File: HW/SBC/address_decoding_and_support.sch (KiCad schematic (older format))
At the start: 9 parts, among them Q1 DS1813, SW1 RESET, U10 74LS138, U15 74LS74, U8 74HCT00, U9 74LS30, X1 8 MHz

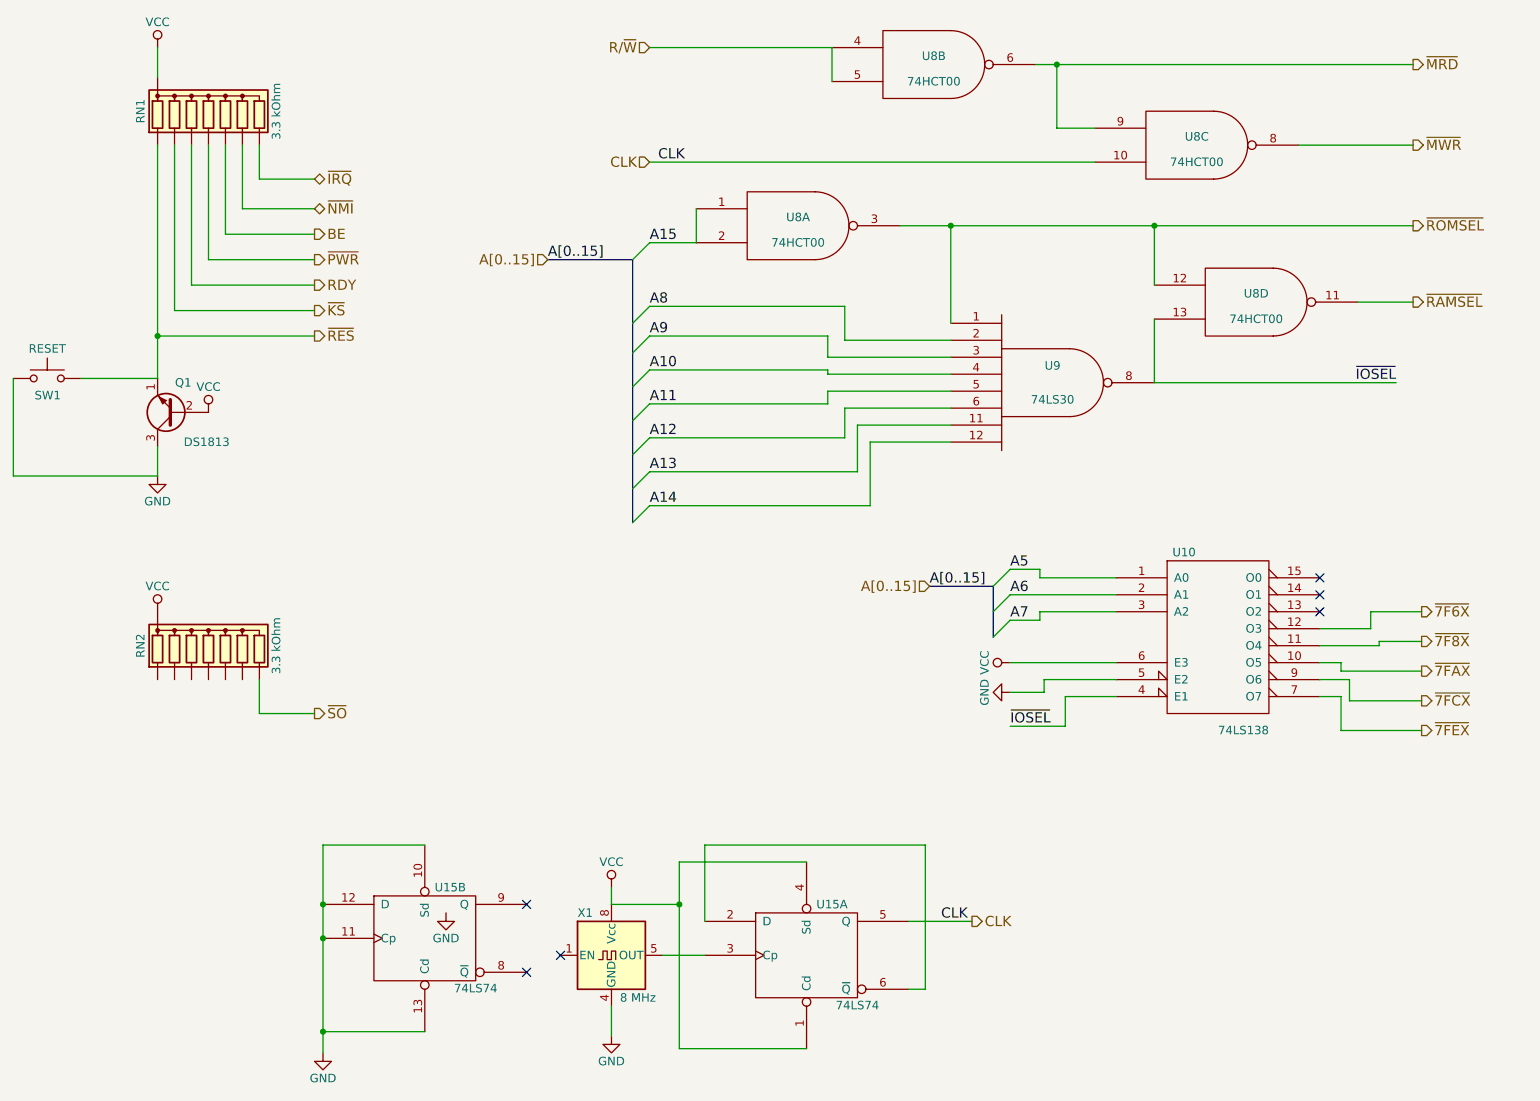
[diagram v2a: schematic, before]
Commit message: Small changes to schematics. Futher development of BIOS.
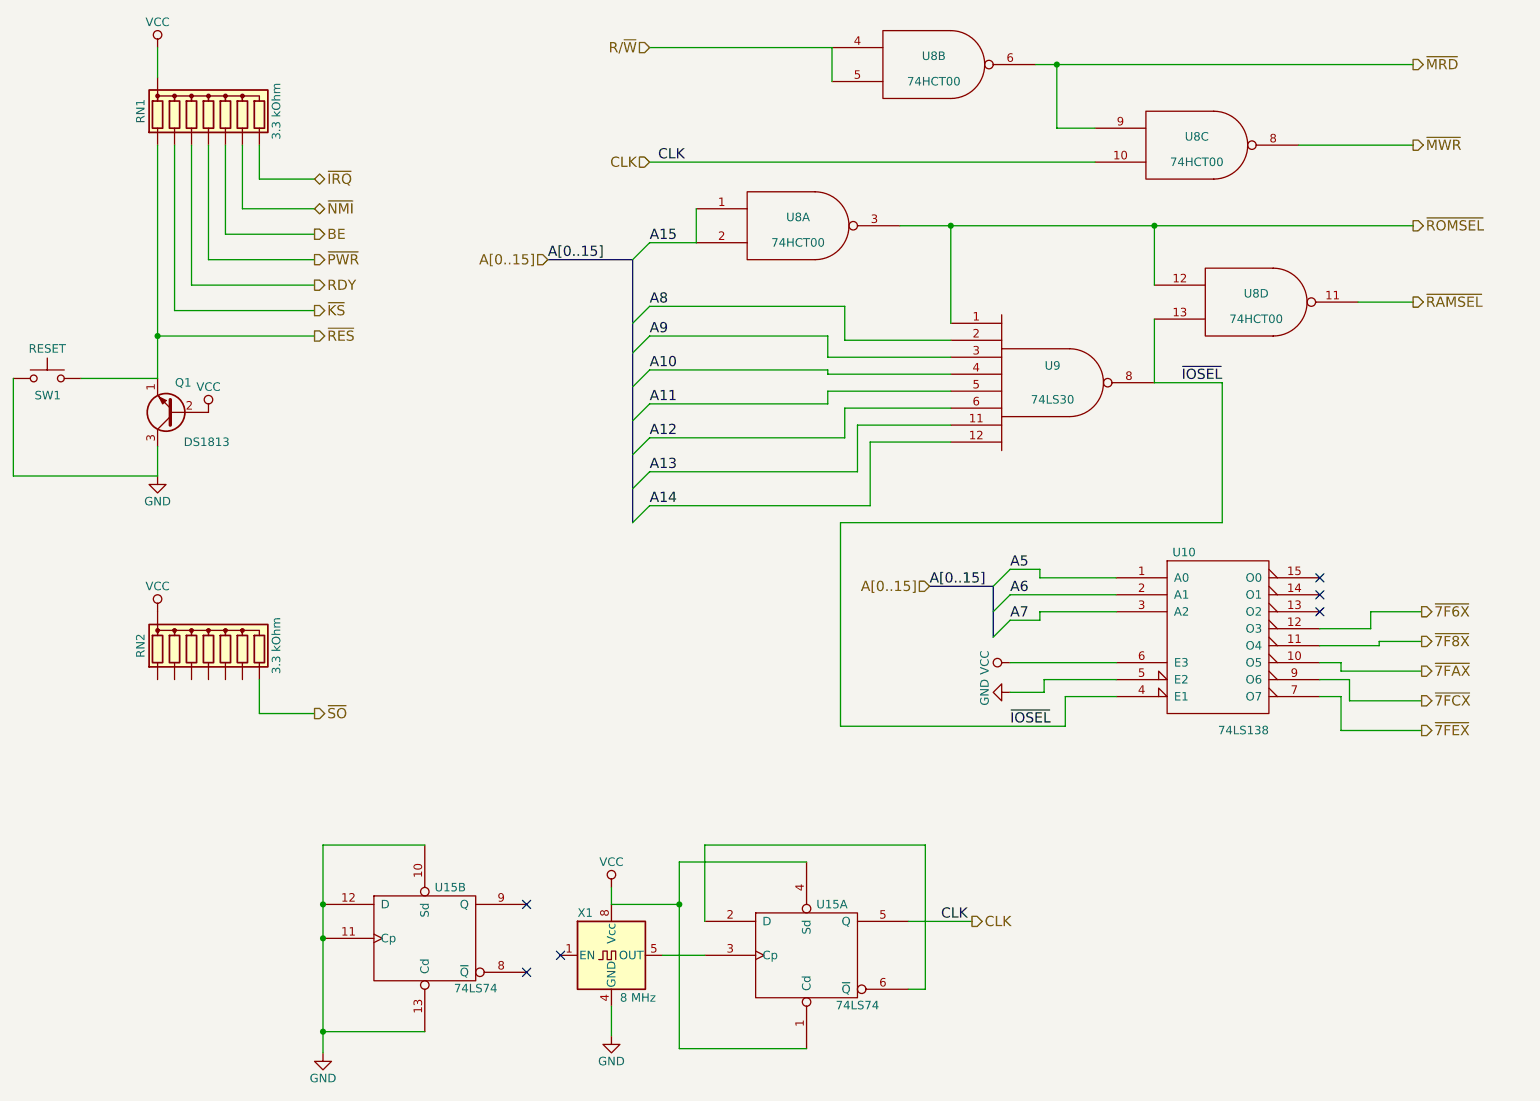
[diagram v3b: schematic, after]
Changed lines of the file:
@@
 LIBS:transistor
 LIBS:uln-ic
-LIBS:IDE_interface
+LIBS:+1.8V
+LIBS:+3.3V
+LIBS:+5V
+LIBS:+9V
+LIBS:25AA02EXXX-XOT
+LIBS:74LVC8T245
+LIBS:4021
+LIBS:7408
+LIBS:74125
+LIBS:74138
+LIBS:74148
+LIBS:74151
+LIBS:74157
+LIBS:74541
+LIBS:ANT
+LIBS:AP6502
+LIBS:AUDIO-JACK-3
+LIBS:AUDIO-JACK-6
+LIBS:BATTERY
+LIBS:BELFUSE-08B0-1X1T-06-F
+LIBS:C
+LIBS:CP
+LIBS:CRYSTAL
+LIBS:CRYSTAL-14
+LIBS:CVAR
+LIBS:DIODE
+LIBS:DIODES-AP3211
+LIBS:DIODESCH
+LIBS:DIODEZENER
+LIBS:DMMT5401
+LIBS:EDISON-BULB-E10
+LIBS:EDISON-SOCKET-E10
+LIBS:ENC28J60
+LIBS:FTDI-PLUG
+LIBS:GNDPWR
+LIBS:~GNDPWR
+LIBS:INDUCTOR
+LIBS:INTEL-EDISON-COMPUTE-MODULE
+LIBS:IS31AP4066D
+LIBS:JTAG
+LIBS:JTAG10
+LIBS:LATTICE-LC4256
+LIBS:LED
+LIBS:LED-BI
+LIBS:LED-BI-COMMON-CATHODE
+LIBS:LM324
+LIBS:LM1875
+LIBS:MAX3221
+LIBS:MC33926
+LIBS:MC34063A
+LIBS:MCP49X1
+LIBS:MCP3204
+LIBS:MECH
+LIBS:MIC2039
+LIBS:MIC2288
+LIBS:MICROSD-AMPHENOL-114-00841-68
+LIBS:MOSFET-N
+LIBS:MOSFET-N-123
+LIBS:MOSFET-N-134
+LIBS:MOSFET-P
+LIBS:NPN
+LIBS:nRF8001
+LIBS:NXPUDA1334ATS
+LIBS:OPAMP-DUAL
+LIBS:P01
+LIBS:P02
+LIBS:P03
+LIBS:P05
+LIBS:P06
+LIBS:P06-MOTOR
+LIBS:P08
+LIBS:P10
+LIBS:P22
+LIBS:P24
+LIBS:PHOTO_TRANSISTOR
+LIBS:PIEZO
+LIBS:PNP
+LIBS:POLYFUSE
+LIBS:POT
+LIBS:PWR_FLAG
+LIBS:QRE1113
+LIBS:R
+LIBS:RASPBERRYPI
+LIBS:RASPBERRYPI2
+LIBS:RBUS8
+LIBS:RN4020
+LIBS:ROBOT-P10-IO
+LIBS:RS-232-DB-9-DTE
+LIBS:SEN-SHT3x-DIS
+LIBS:SERVO
+LIBS:SI4737-C40-GM
+LIBS:SI4737-GU
+LIBS:SKYWORKS-AAT1217-3.3
+LIBS:SPDT
+LIBS:SPST
+LIBS:SPST-4PIN
+LIBS:SST25VF032B-S2A
+LIBS:SST26VF032B
+LIBS:ST-LIS3MDL
+LIBS:STM32-32PIN
+LIBS:STM32-48PIN
+LIBS:STM32-64PIN
+LIBS:STM32SWDUART
+LIBS:ST-SWD
+LIBS:ST-TDA7266
+LIBS:SWD
+LIBS:TCS3472
+LIBS:TI-ADS7866
+LIBS:TICC3000
+LIBS:TIREF30XX
+LIBS:TP
+LIBS:TS5A623157
+LIBS:TSV631
+LIBS:TVS-DIODE
+LIBS:TXB0108-PW
+LIBS:USBAB
+LIBS:Vcc
+LIBS:Vdd
+LIBS:VIN
+LIBS:VREG
+LIBS:VREG_VOUTCENTER
 LIBS:74xgxx
 LIBS:ac-dc
@@
 Text HLabel 9075 2600 2    60   Output ~ 0
 ~RAMSEL
-Text Label 8975 3075 2    60   ~ 0
+Text Label 7950 3075 2    60   ~ 0
 ~IOSEL
 Text Label 6700 5100 0    60   ~ 0
@@
 Connection ~ 7550 2150
 Wire Wire Line
-	7550 3075 8975 3075
+	7550 3075 7950 3075
 Wire Wire Line
 	7550 3075 7550 2700
@@
 	7025 4925 7025 5100
 Wire Wire Line
-	7025 5100 6700 5100
+	7025 5100 5700 5100
 Wire Wire Line
 	6900 4825 6900 4900
@@
 	3250 6900 2650 6900
 Connection ~ 2650 6900
-$Comp
-L GND #PWR37
-U 1 1 5948F014
-P 3375 6200
-F 0 "#PWR37" H 3375 5950 50  0001 C CNN
-F 1 "GND" H 3375 6050 50  0000 C CNN
-F 2 "" H 3375 6200 50  0001 C CNN
-F 3 "" H 3375 6200 50  0001 C CNN
-	1    3375 6200
-	1    0    0    -1
-$EndComp
 Text HLabel 2600 2650 2    60   Output ~ 0
 ~KS
@@
 	2275 5025 2600 5025
 $Comp
-L VCC #PWR?
+L VCC #PWR33
 U 1 1 594C1459
 P 1675 1100
-F 0 "#PWR?" H 1675 950 50  0001 C CNN
+F 0 "#PWR33" H 1675 950 50  0001 C CNN
 F 1 "VCC" H 1675 1250 50  0000 C CNN
 F 2 "" H 1675 1100 50  0001 C CNN
@@
 $EndComp
 $Comp
-L GND #PWR?
+L GND #PWR37
 U 1 1 595DE156
 P 2650 7025
-F 0 "#PWR?" H 2650 6775 50  0001 C CNN
+F 0 "#PWR37" H 2650 6775 50  0001 C CNN
 F 1 "GND" H 2650 6875 50  0000 C CNN
 F 2 "" H 2650 7025 50  0001 C CNN
@@
 NoConn ~ 3850 6550
 NoConn ~ 4050 6450
+Wire Wire Line
+	7950 3075 7950 3900
+Wire Wire Line
+	7950 3900 5700 3900
+Wire Wire Line
+	5700 3900 5700 5100
 $EndSCHEMATC

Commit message: Changed all TTLs to HC family.
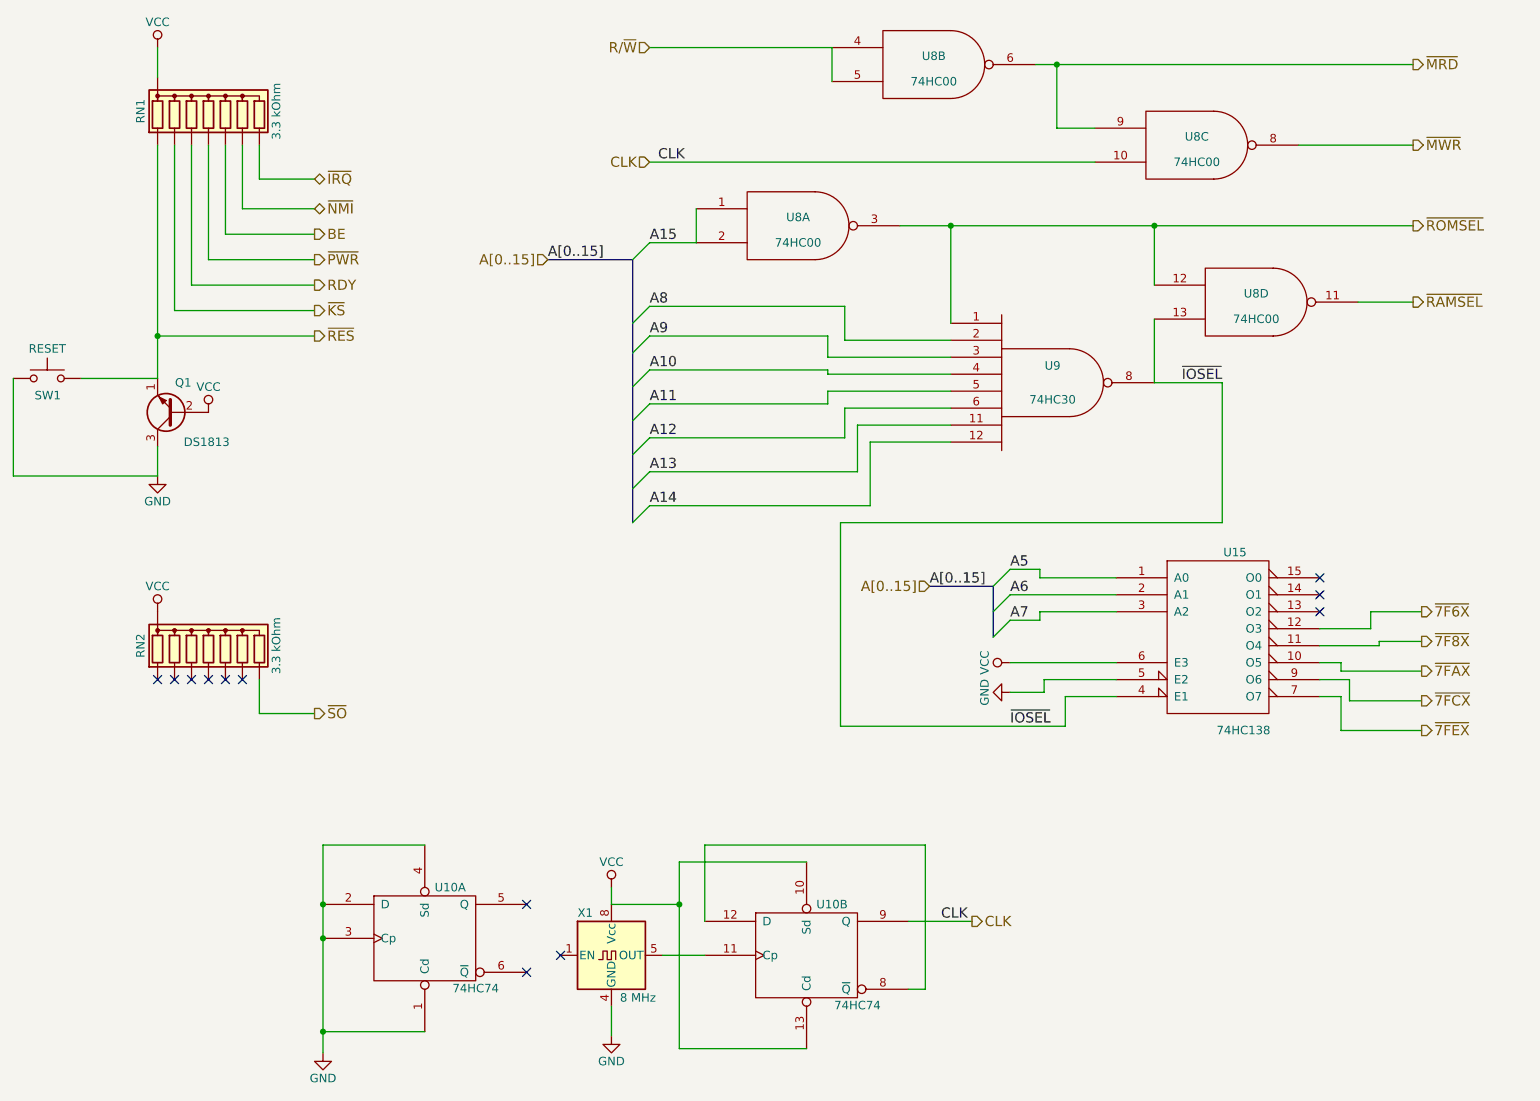
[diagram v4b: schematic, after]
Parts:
- removed U10: 74LS138, Housings_DIP:DIP-16_W7.62mm_Socket, symbol 74LS138
- removed U15: 74LS74, Housings_DIP:DIP-14_W7.62mm_Socket, symbol 74LS74
- removed U8: 74HCT00, Housings_DIP:DIP-14_W7.62mm_Socket, symbol 74HCT00
- removed U9: 74LS30, Housings_DIP:DIP-14_W7.62mm_Socket, symbol 74LS30
- added U10: 74HC74, symbol 74HC74
- added U15: 74HC138, symbol 74HC138
- added U8: 74HC00, symbol 74HC00
- added U9: 74HC30, symbol 74HC30
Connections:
- net A10: now also U9.4
- net A11: now also U9.5
- net A12: now also U9.6
- net A13: now also U9.11
- net A14: now also U9.12
- net A15: now also U8.1, U8.2
- net A5: now also U15.1 (A0)
- net A6: now also U15.2 (A1)
- net A7: now also U15.3 (A2)
- net A8: now also U9.2
- net A9: now also U9.3
- net CLK: now also U10.9 (Q), U8.10
- net GND: now also U10.1 (Cd), U10.2 (D), U10.3 (Cp), U10.4 (Sd), U10.7 (GND), U10.7 (GND), U15.5 (E2), U15.8 (GND), U8.7 (GND), U8.7 (GND), U8.7 (GND), U8.7 (GND), U9.7 (GND)
- net R/~W: now also U8.4, U8.5
- net VCC: now also U10.10 (Sd), U10.13 (Cd), U10.14 (VCC), U10.14 (VCC), U15.16 (VCC), U15.6 (E3), U8.14 (VCC), U8.14 (VCC), U8.14 (VCC), U8.14 (VCC), U9.14 (VCC)
- net ~7F6X: now also U15.12 (O3)
- net ~7F8X: now also U15.11 (O4)
- net ~7FAX: now also U15.10 (O5)
- net ~7FCX: now also U15.9 (O6)
- net ~7FEX: now also U15.7 (O7)
- net ~IOSEL: now also U15.4 (E1), U8.13, U9.8
- net ~MRD: now also U8.6, U8.9
- net ~MWR: now also U8.8
- net ~RAMSEL: now also U8.11
- net ~ROMSEL: now also U8.12, U8.3, U9.1
- net at X1.5 (OUT): now also U10.11 (Cp)
- new net: U10.12 (D), U10.8 (~Q)
- no-connect marks 6 -> 12
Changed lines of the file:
@@
 $EndDescr
-$Comp
-L 74HCT00 U8
-U 1 1 58D59B66
-P 5450 2150
-F 0 "U8" H 5450 2200 50  0000 C CNN
-F 1 "74HCT00" H 5450 2050 50  0000 C CNN
-F 2 "Housings_DIP:DIP-14_W7.62mm_Socket" H 5450 2150 50  0001 C CNN
-F 3 "" H 5450 2150 50  0001 C CNN
-	1    5450 2150
-	1    0    0    -1
-$EndComp
-$Comp
-L 74HCT00 U8
-U 4 1 58D59B7D
-P 8150 2600
-F 0 "U8" H 8150 2650 50  0000 C CNN
-F 1 "74HCT00" H 8150 2500 50  0000 C CNN
-F 2 "Housings_DIP:DIP-14_W7.62mm_Socket" H 8150 2600 50  0001 C CNN
-F 3 "" H 8150 2600 50  0001 C CNN
-	4    8150 2600
-	1    0    0    -1
-$EndComp
-$Comp
-L 74HCT00 U8
-U 2 1 58D59C3A
-P 6250 1200
-F 0 "U8" H 6250 1250 50  0000 C CNN
-F 1 "74HCT00" H 6250 1100 50  0000 C CNN
-F 2 "Housings_DIP:DIP-14_W7.62mm_Socket" H 6250 1200 50  0001 C CNN
-F 3 "" H 6250 1200 50  0001 C CNN
-	2    6250 1200
-	1    0    0    -1
-$EndComp
-$Comp
-L 74HCT00 U8
-U 3 1 58D59CAD
-P 7800 1675
-F 0 "U8" H 7800 1725 50  0000 C CNN
-F 1 "74HCT00" H 7800 1575 50  0000 C CNN
-F 2 "Housings_DIP:DIP-14_W7.62mm_Socket" H 7800 1675 50  0001 C CNN
-F 3 "" H 7800 1675 50  0001 C CNN
-	3    7800 1675
-	1    0    0    -1
-$EndComp
-$Comp
-L 74LS30 U9
-U 1 1 58D59CF0
-P 6950 3075
-F 0 "U9" H 6950 3175 50  0000 C CNN
-F 1 "74LS30" H 6950 2975 50  0000 C CNN
-F 2 "Housings_DIP:DIP-14_W7.62mm_Socket" H 6950 3075 50  0001 C CNN
-F 3 "" H 6950 3075 50  0001 C CNN
-	1    6950 3075
-	1    0    0    -1
-$EndComp
-$Comp
-L 74LS138 U10
-U 1 1 58D59D0F
-P 7925 4575
-F 0 "U10" H 7725 5075 50  0000 C CNN
-F 1 "74LS138" H 8075 4026 50  0000 C CNN
-F 2 "Housings_DIP:DIP-16_W7.62mm_Socket" H 7925 4575 50  0001 C CNN
-F 3 "" H 7925 4575 50  0001 C CNN
-	1    7925 4575
-	1    0    0    -1
-$EndComp
 $Comp
 L R_Network07 RN1
@@
 	1    6700 4900
 	0    1    1    0
-$EndComp
-$Comp
-L 74LS74 U15
-U 1 1 593140EB
-P 5500 6450
-F 0 "U15" H 5650 6750 50  0000 C CNN
-F 1 "74LS74" H 5800 6155 50  0000 C CNN
-F 2 "Housings_DIP:DIP-14_W7.62mm_Socket" H 5500 6450 50  0001 C CNN
-F 3 "" H 5500 6450 50  0001 C CNN
-	1    5500 6450
-	1    0    0    -1
 $EndComp
 Text Label 6450 6250 2    60   ~ 0
@@
 NoConn ~ 8525 4325
 NoConn ~ 8525 4225
-$Comp
-L 74LS74 U15
-U 2 1 5948E1C2
-P 3250 6350
-F 0 "U15" H 3400 6650 50  0000 C CNN
-F 1 "74LS74" H 3550 6055 50  0000 C CNN
-F 2 "" H 3250 6350 50  0001 C CNN
-F 3 "" H 3250 6350 50  0001 C CNN
-	2    3250 6350
-	1    0    0    -1
-$EndComp
 Wire Wire Line
 	6050 2150 9075 2150
@@
 Wire Wire Line
 	5700 3900 5700 5100
+NoConn ~ 2075 4825
+NoConn ~ 1975 4825
+NoConn ~ 1875 4825
+NoConn ~ 1775 4825
+NoConn ~ 1675 4825
+NoConn ~ 2175 4825
+$Comp
+L 74HC30 U9
+U 1 1 5A42B90E
+P 6950 3075
+F 0 "U9" H 6950 3175 50  0000 C CNN
+F 1 "74HC30" H 6950 2975 50  0000 C CNN
+F 2 "" H 6950 3075 50  0001 C CNN
+F 3 "" H 6950 3075 50  0001 C CNN
+	1    6950 3075
+	1    0    0    -1
+$EndComp
+$Comp
+L 74HC00 U8
+U 1 1 5A42BF1B
+P 5450 2150
+F 0 "U8" H 5450 2200 50  0000 C CNN
+F 1 "74HC00" H 5450 2050 50  0000 C CNN
+F 2 "" H 5450 2150 50  0001 C CNN
+F 3 "" H 5450 2150 50  0001 C CNN
+	1    5450 2150
+	1    0    0    -1
+$EndComp
+$Comp
+L 74HC00 U8
+U 2 1 5A42C03A
+P 6250 1200
+F 0 "U8" H 6250 1250 50  0000 C CNN
+F 1 "74HC00" H 6250 1100 50  0000 C CNN
+F 2 "" H 6250 1200 50  0001 C CNN
+F 3 "" H 6250 1200 50  0001 C CNN
+	2    6250 1200
+	1    0    0    -1
+$EndComp
+$Comp
+L 74HC00 U8
+U 3 1 5A42C0DB
+P 7800 1675
+F 0 "U8" H 7800 1725 50  0000 C CNN
+F 1 "74HC00" H 7800 1575 50  0000 C CNN
+F 2 "" H 7800 1675 50  0001 C CNN
+F 3 "" H 7800 1675 50  0001 C CNN
+	3    7800 1675
+	1    0    0    -1
+$EndComp
+$Comp
+L 74HC00 U8
+U 4 1 5A42C128
+P 8150 2600
+F 0 "U8" H 8150 2650 50  0000 C CNN
+F 1 "74HC00" H 8150 2500 50  0000 C CNN
+F 2 "" H 8150 2600 50  0001 C CNN
+F 3 "" H 8150 2600 50  0001 C CNN
+	4    8150 2600
+	1    0    0    -1
+$EndComp
+$Comp
+L 74HC138 U15
+U 1 1 5A42D7A7
+P 7925 4575
+F 0 "U15" H 8025 5075 50  0000 C CNN
+F 1 "74HC138" H 8075 4026 50  0000 C CNN
+F 2 "" H 7925 4575 50  0001 C CNN
+F 3 "" H 7925 4575 50  0001 C CNN
+	1    7925 4575
+	1    0    0    -1
+$EndComp
+$Comp
+L 74HC74 U10
+U 2 1 5A42E08B
+P 5500 6450
+F 0 "U10" H 5650 6750 50  0000 C CNN
+F 1 "74HC74" H 5800 6155 50  0000 C CNN
+F 2 "" H 5500 6450 50  0001 C CNN
+F 3 "" H 5500 6450 50  0001 C CNN
+	2    5500 6450
+	1    0    0    -1
+$EndComp
+$Comp
+L 74HC74 U10
+U 1 1 5A42E0C8
+P 3250 6350
+F 0 "U10" H 3400 6650 50  0000 C CNN
+F 1 "74HC74" H 3550 6055 50  0000 C CNN
+F 2 "" H 3250 6350 50  0001 C CNN
+F 3 "" H 3250 6350 50  0001 C CNN
+	1    3250 6350
+	1    0    0    -1
+$EndComp
 $EndSCHEMATC
